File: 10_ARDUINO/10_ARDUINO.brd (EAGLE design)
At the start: 67.4 x 44.8 mm, 3 parts, among them M1 ARDUINO_PROMINI, X1 ALLSERIALSLAVE

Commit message: Revert "pro mini layout corrected"
This reverts commit e6acf7b114fc184efa746b3a51c54623d1353390.
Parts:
- removed SJ1: (no value), jumper:SJ_2
- added JP1: (no value), jumper:JP2
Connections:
- net N$279: now also JP1.1, X1.20; no longer SJ1.3, X1.2
- net N$280: now also JP1.3, X1.2; no longer SJ1.1, X1.20
- net VCC: now also JP1.2; no longer SJ1.2
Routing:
- net N$279: track 7.99 -> 4.07 mm
- net VCC: track 68.5 -> 64.8 mm
- net N$280: track 4.49 -> 7.51 mm
- net N$2: track 22.6 -> 21.4 mm
- net N$11: track 30.0 -> 28.8 mm
- net N$1: track 5.23 -> 3.96 mm
- removed copper zone on layer 1, net N$10
- removed copper zone on layer 1, net N$100
- removed copper zone on layer 1, net N$101
- removed copper zone on layer 1, net N$102
- removed copper zone on layer 1, net N$103
- removed copper zone on layer 1, net N$104
- removed copper zone on layer 1, net N$105
- removed copper zone on layer 1, net N$106
- removed copper zone on layer 1, net N$107
- removed copper zone on layer 16, net N$245
- removed copper zone on layer 16, net N$246
- removed copper zone on layer 16, net N$247
- removed copper zone on layer 16, net N$248
- removed copper zone on layer 16, net N$249
- removed copper zone on layer 16, net N$250
- removed copper zone on layer 16, net N$251
- removed copper zone on layer 16, net N$252
- removed copper zone on layer 16, net N$253
- removed copper zone on layer 16, net N$254
- removed copper zone on layer 16, net N$255
- removed copper zone on layer 16, net N$256
- removed copper zone on layer 16, net N$257
- removed copper zone on layer 16, net N$258
- removed copper zone on layer 16, net N$259
- removed copper zone on layer 16, net N$260
- removed copper zone on layer 1, net N$276
- removed copper zone on layer 1, net N$277
- removed copper zone on layer 1, net N$278
- removed copper zone on layer 1, net N$281
- removed copper zone on layer 1, net N$282
- removed copper zone on layer 16, net N$283
- removed copper zone on layer 16, net N$284
- removed copper zone on layer 16, net N$285
- removed copper zone on layer 16, net N$286
- removed copper zone on layer 16, net N$287
- removed copper zone on layer 16, net N$288
- removed copper zone on layer 16, net N$292
- removed copper zone on layer 1, net N$3
- removed copper zone on layer 1, net N$4
- removed copper zone on layer 1, net N$5
- removed copper zone on layer 1, net N$6
- removed copper zone on layer 1, net N$7
- removed copper zone on layer 1, net N$8
- removed copper zone on layer 1, net N$9
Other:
- board text added: "AllSerial Arduino v1.0 43/18"
- board text removed: "AllSerial Arduino v1.1 45/18"

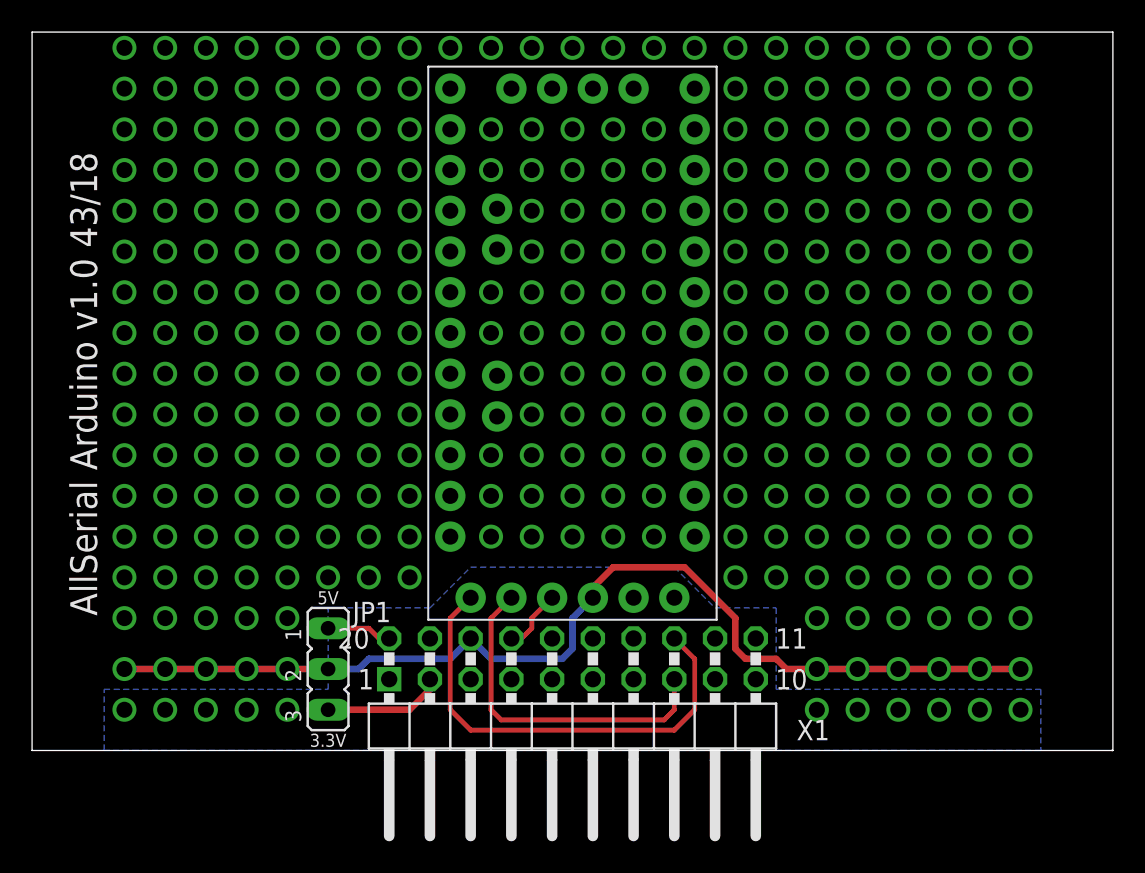
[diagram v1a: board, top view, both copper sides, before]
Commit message: pro mini layout corrected
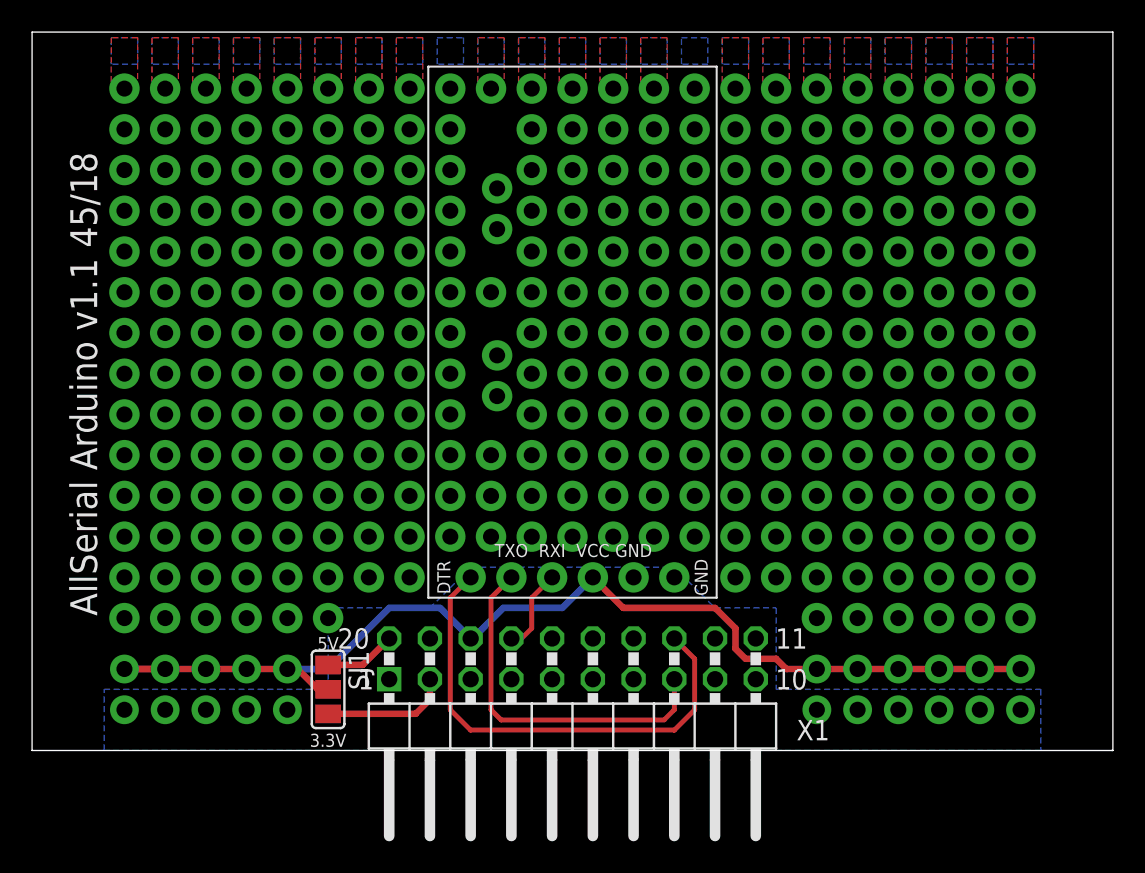
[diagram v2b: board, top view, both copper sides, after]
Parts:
- removed JP1: (no value), jumper:JP2
- added SJ1: (no value), jumper:SJ_2
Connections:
- net N$279: now also SJ1.3, X1.2; no longer JP1.1, X1.20
- net N$280: now also SJ1.1, X1.20; no longer JP1.3, X1.2
- net VCC: now also SJ1.2; no longer JP1.2
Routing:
- net N$279: track 4.07 -> 7.99 mm
- net VCC: track 64.8 -> 68.5 mm
- net N$280: track 7.51 -> 4.49 mm
- net N$2: track 21.4 -> 22.6 mm
- net N$11: track 28.8 -> 30.0 mm
- net N$1: track 3.96 -> 5.23 mm
- added copper zone on layer 1, net N$10
- added copper zone on layer 1, net N$100
- added copper zone on layer 1, net N$101
- added copper zone on layer 1, net N$102
- added copper zone on layer 1, net N$103
- added copper zone on layer 1, net N$104
- added copper zone on layer 1, net N$105
- added copper zone on layer 1, net N$106
- added copper zone on layer 1, net N$107
- added copper zone on layer 16, net N$245
- added copper zone on layer 16, net N$246
- added copper zone on layer 16, net N$247
- added copper zone on layer 16, net N$248
- added copper zone on layer 16, net N$249
- added copper zone on layer 16, net N$250
- added copper zone on layer 16, net N$251
- added copper zone on layer 16, net N$252
- added copper zone on layer 16, net N$253
- added copper zone on layer 16, net N$254
- added copper zone on layer 16, net N$255
- added copper zone on layer 16, net N$256
- added copper zone on layer 16, net N$257
- added copper zone on layer 16, net N$258
- added copper zone on layer 16, net N$259
- added copper zone on layer 16, net N$260
- added copper zone on layer 1, net N$276
- added copper zone on layer 1, net N$277
- added copper zone on layer 1, net N$278
- added copper zone on layer 1, net N$281
- added copper zone on layer 1, net N$282
- added copper zone on layer 16, net N$283
- added copper zone on layer 16, net N$284
- added copper zone on layer 16, net N$285
- added copper zone on layer 16, net N$286
- added copper zone on layer 16, net N$287
- added copper zone on layer 16, net N$288
- added copper zone on layer 16, net N$292
- added copper zone on layer 1, net N$3
- added copper zone on layer 1, net N$4
- added copper zone on layer 1, net N$5
- added copper zone on layer 1, net N$6
- added copper zone on layer 1, net N$7
- added copper zone on layer 1, net N$8
- added copper zone on layer 1, net N$9
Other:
- board text added: "AllSerial Arduino v1.1 45/18"
- board text removed: "AllSerial Arduino v1.0 43/18"
